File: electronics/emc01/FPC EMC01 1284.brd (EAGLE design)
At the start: 160 x 100 mm, 93 parts, among them J4 PCIE, Q1 RFP30N06LE, Q2 RFP30N06LE, Q3 RFP30N06LE, SW1 SPST_TACT-EVQQ2, U1 LM2841, U10 MCP4728, U2 A4982, U3 A4982, U4 A4982, U5 ATMEGA1284P-AU, U7 AP7313, X1 Camera FFC

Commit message: Added modular tool connectors, RasPi connector, Front Panel connector. 
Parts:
- removed D2: (no value), printrbot:SMA
- removed F1: (no value), printrbot:MINISMDC
- removed JP17: FAN, SparkFun:1X02
- removed JP2: LCD HEADER, pinhead-2:2X08SMD
- removed JP5: RPI GPIO, pinhead-2:2X13SMD
- removed JP6: HOTEND, SRG:JST_B4B-PH_HEADER
- removed MS-X, MS-Y, MS-Z: (no value), printrbot:SJ_3_CONNECTED
- removed Q1, Q2: RFP30N06LE, SparkFun:TO220V
- removed Q3: RFP30N06LE, ipc-7351-transistor:SOT95P280X135-3N
- removed R11, R36: 100, adafruit:R0805
- removed R14, R35, R6: 100k, adafruit:R0805
- removed X1: Camera FFC, con-hirose:FH12-15S-0.5SH
- added J1, J3, J5, J6, J7: (no value), !con-lstb:MA08-2
- added J11: (no value), !con-lstb:MA06-1
- added J12: (no value), !con-lstb:MA02-1
- added J8: CON-HDMI, !NJ SMT:CON-HDMI-FCI-10029449-001RLF
- added J9: CON-FFC-SFW15R, !NJ SMT:CON-FFC-SFW15R
- J2: device printrbot:PHOENIX-5MM-2POS -> !con-lstb:MA13-2
- moved J2 263.9 mm to (-125.7, -219.7)
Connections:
- net XYZENABLE renamed /XYZENABLE
- removed net !HOTBED: R11.1, R35.1
- removed net !HOTEND: R36.1, R6.1
- removed net !PWM-FAN: Q3.1, R14.1
- removed net B-THERM: U5.36
- removed net E-THERM: U5.37
- removed net HOTBED-GND: J2.P$2, Q2.2
- removed net HOTEND-GND: JP6.P1, JP6.P2, Q1.2
- removed net N$2: D2.C, F1.P$2, Q3.3
- removed net N$27: MS-X.1, U2.5
- removed net N$28: MS-X.3, U2.6
- removed net N$42: MS-Y.1, U3.5
- removed net N$43: MS-Y.3, U3.6
- removed net N$5: F1.P$1, JP17.2
- removed net N$57: MS-Z.1, U4.5
- removed net N$58: MS-Z.3, U4.6
- removed net N$7: Q2.1, R11.2
- removed net N$71: Q1.1, R36.2
- removed net PD0-RX1: U5.9
- removed net PD1-TX1: U5.10
- removed net SCK: U5.3
- removed net TOOL-DIR: U5.40
- removed net TOOL-STEP: U5.41
- removed net TOOL1-DOUT: U5.33
- removed net TOOL1-ENABLE: U5.14
- removed net TOOL2-DOUT: U5.32
- removed net TOOL2-ENABLE: U5.13
- removed net TOOL3-DOUT: U5.31
- removed net TOOL3-ENABLE: U5.12
- removed net TOOL4-AIN: U5.34
- removed net TOOL4-DOUT: U5.30
- removed net TOOL4-ENABLE: U5.11
- removed net VREF_E: U10.6
- removed net Z-ENABLE: U5.35
- new net +3V3_RASPI: J2.1, J2.17, J7.2
- new net AVR_RXD: J11.3, U5.9
- new net AVR_TXD: J11.2, U5.10
- new net DTR: J11.1
- new net LCD_/E: J2.18, J7.7
- new net LCD_DB4: J2.16, J7.9
- new net LCD_DB5: J2.11, J7.10
- new net LCD_DB6: J2.13, J7.11
- new net LCD_DB7: J2.15, J7.12
- new net LCD_RS: J2.22, J7.8
- new net PANEL_ENC_A: J2.26, J7.5
- new net PANEL_ENC_B: J2.21, J7.6
- new net PANEL_ENC_SW: J2.24, J7.4
- new net PANEL_LED_GRN: J2.19, J7.13
- new net PANEL_LED_RED: J2.12, J7.14
- new net PANEL_PUSHBTN: J2.23, J7.15
- new net RASPI_RXD: J12.1, J2.10
- new net RASPI_TXD: J12.2, J2.8
- new net TOOL1_AIN: J1.13, U5.37
- new net TOOL1_DOUT: J1.12, U5.33
- new net TOOL1_ENABLE: J1.9, U5.14
- new net TOOL2_AIN: J3.13, U5.36
- new net TOOL2_DOUT: J3.12, U5.32
- new net TOOL2_ENABLE: J3.9, U5.13
- new net TOOL3_AIN: J5.13, U5.35
- new net TOOL3_DOUT: J5.12, U5.31
- new net TOOL3_ENABLE: J5.9, U5.12
- new net TOOL4_AIN: J6.13, U5.34
- new net TOOL4_DOUT: J6.12, U5.30
- new net TOOL4_ENABLE: J6.9, U5.11
- new net TOOL_DIR: J1.11, J3.11, J5.11, J6.11, U5.40
- new net TOOL_STEP: J1.10, J3.10, J5.10, J6.10, U5.41
- new net Z_DIR: U5.42
- new net Z_STEP: U5.43
- net +5V: now also J1.14, J11.4, J2.2, J2.4, J3.14, J3.7, J5.14, J5.8, J6.14, J6.7, J6.8, J7.1, U2.5, U2.6, U3.5, U3.6, U4.5, U4.6; no longer MS-X.2, MS-Y.2, MS-Z.2
- net 12V: now also J1.1, J1.2, J3.1, J3.2, J5.1, J5.2, J6.1, J6.2; no longer J2.P$1, JP17.1, JP6.P3, JP6.P4
- net GND: now also J1.15, J1.16, J1.3, J1.4, J1.7, J1.8, J11.5, J11.6, J2.14, J2.20, J2.25, J2.6, J2.9, J3.15, J3.16, J3.3, J3.4, J3.8, J5.15, J5.16, J5.3, J5.4, J5.7, J6.15, J6.16, J6.3, J6.4, J7.16, J7.3; no longer D2.A, Q1.3, Q2.3, Q3.2, R14.2, R35.2, R6.2
- net SCL: now also J1.6, J3.6, J5.6, J6.6
- net SCLK: now also U5.3
- net SDA: now also J1.5, J3.5, J5.5, J6.5
- net Z-DIR: no longer U5.42
- net Z-STEP: no longer U5.43

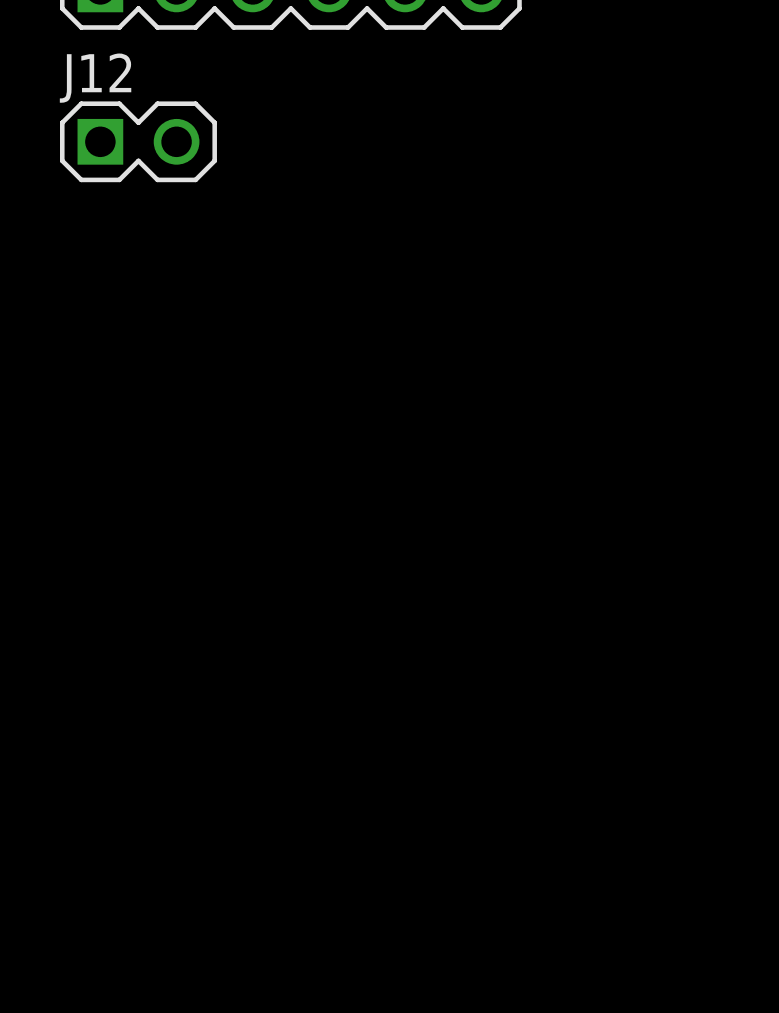
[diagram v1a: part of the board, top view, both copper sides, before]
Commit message: adding Dayton's 5958 ICSP/Power circuits to Neil's board
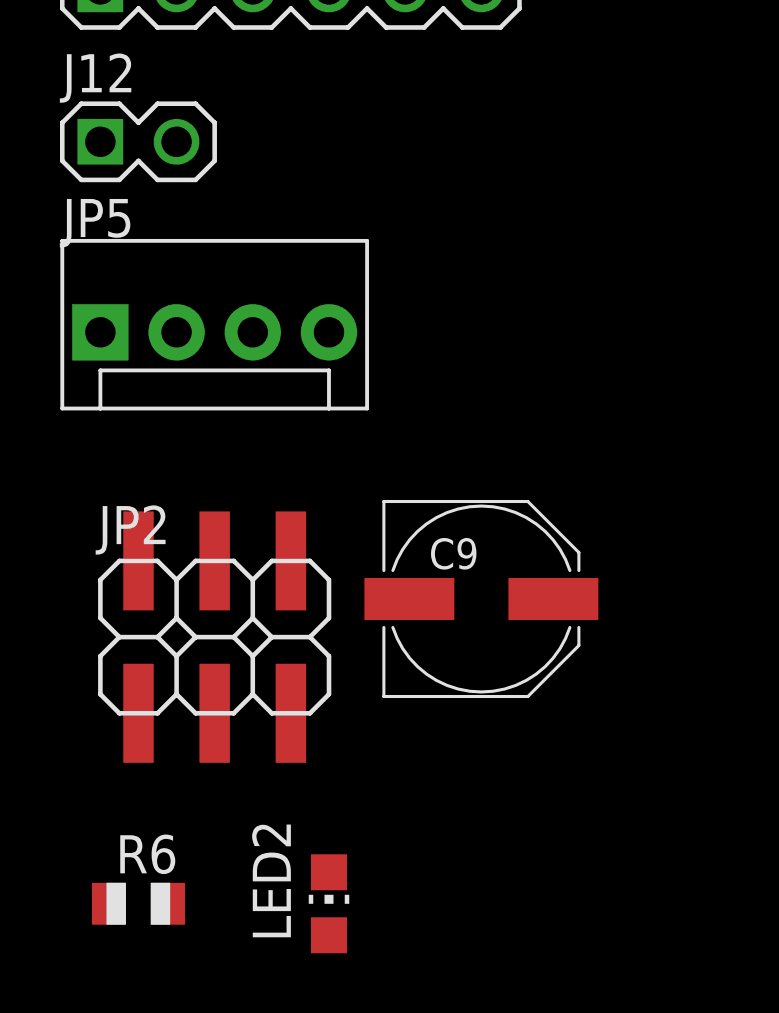
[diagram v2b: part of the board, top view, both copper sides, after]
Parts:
- added C9: 100uF, rcl:PANASONIC_D
- added JP2: ICSP, pinhead-2:2X03SMD
- added JP5: I2C, SparkFun:MOLEX-1X4
- added LED2: PWR, led:CHIP-LED0805
- added R6: 330, adafruit:R0805
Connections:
- net !RESET: now also JP2.2
- net +5V: now also JP2.5, JP5.4, R6.2
- net 12V: now also C9.+
- net GND: now also C9.-, JP2.1, JP5.3, LED2.C
- net MISO: now also JP2.6
- net MOSI: now also JP2.3
- net SCL: now also JP5.1
- net SCLK: now also JP2.4
- net SDA: now also JP5.2
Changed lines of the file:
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@@
 <?xml version="1.0" encoding="utf-8"?>
 <!DOCTYPE eagle SYSTEM "eagle.dtd">
-<eagle version="6.6.0">
+<eagle version="6.5.0">
 <drawing>
 <settings>
@@
 <element name="J11" library="!con-lstb" package="MA06-1" value="" x="-135.89" y="-257.81"/>
 <element name="J12" library="!con-lstb" package="MA02-1" value="" x="-140.97" y="-262.89"/>
+<element name="R6" library="adafruit" package="R0805" value="330" x="-140.97" y="-288.29"/>
+<element name="LED2" library="led" package="CHIP-LED0805" value="PWR" x="-134.62" y="-288.29"/>
+<element name="JP2" library="pinhead-2" package="2X03SMD" value="ICSP" x="-139.7" y="-278.13"/>
+<element name="C9" library="rcl" package="PANASONIC_D" value="100uF" x="-129.54" y="-278.13"/>
+<element name="JP5" library="SparkFun" package="MOLEX-1X4" value="I2C" x="-142.24" y="-269.24"/>
 </elements>
 <signals>
@@
 <contactref element="J11" pad="5"/>
 <contactref element="J11" pad="6"/>
+<contactref element="C9" pad="-"/>
+<contactref element="JP2" pad="1"/>
+<contactref element="LED2" pad="C"/>
+<contactref element="JP5" pad="3"/>
 <wire x1="-122.92" y1="-48.6" x2="-124.09" y2="-58.42" width="0" layer="19" extent="1-1"/>
 <wire x1="-103.82" y1="-26.67" x2="-122.92" y2="-48.6" width="0" layer="19" extent="1-1"/>
@@
 <wire x1="-132.08" y1="-257.81" x2="-138.43" y2="-228.6" width="0" layer="19" extent="1-1"/>
 <wire x1="-129.54" y1="-257.81" x2="-132.08" y2="-257.81" width="0" layer="19" extent="1-1"/>
+<wire x1="-137.16" y1="-269.24" x2="-132.08" y2="-257.81" width="0" layer="19" extent="1-1"/>
+<wire x1="-131.94" y1="-278.13" x2="-137.16" y2="-269.24" width="0" layer="19" extent="1-1"/>
+<wire x1="-134.62" y1="-287.24" x2="-131.94" y2="-278.13" width="0" layer="19" extent="1-1"/>
+<wire x1="-140.97" y1="-281.94" x2="-134.62" y2="-287.24" width="0" layer="19" extent="1-1"/>
 </signal>
 <signal name="!RESET">
 <contactref element="JP4" pad="2"/>
+<contactref element="JP2" pad="2"/>
+<wire x1="-78.74" y1="7.62" x2="-140.97" y2="-276.86" width="0" layer="19" extent="1-1"/>
 </signal>
 <signal name="12V">
@@
 <contactref element="J6" pad="1"/>
 <contactref element="J6" pad="2"/>
+<contactref element="C9" pad="+"/>
+<wire x1="-140.97" y1="-213.36" x2="-127.14" y2="-278.13" width="0" layer="19" extent="1-1"/>
 <wire x1="-140.97" y1="-210.82" x2="-140.97" y2="-213.36" width="0" layer="19" extent="1-1"/>
 <wire x1="-140.97" y1="-205.74" x2="-140.97" y2="-210.82" width="0" layer="19" extent="1-1"/>
@@
 <contactref element="JP4" pad="6"/>
 <contactref element="U5" pad="2"/>
-<wire x1="-73.66" y1="7.62" x2="72.417896875" y2="21.063946875" width="0" layer="19" extent="1-1"/>
+<contactref element="JP2" pad="6"/>
+<wire x1="-73.66" y1="7.62" x2="-135.89" y2="-276.86" width="0" layer="19" extent="1-1"/>
+<wire x1="72.417896875" y1="21.063946875" x2="-73.66" y2="7.62" width="0" layer="19" extent="1-1"/>
 </signal>
 <signal name="MOSI">
 <contactref element="JP4" pad="3"/>
 <contactref element="U5" pad="1"/>
-<wire x1="-76.2" y1="2.54" x2="71.861121875" y2="21.620721875" width="0" layer="19" extent="1-1"/>
+<contactref element="JP2" pad="3"/>
+<wire x1="-76.2" y1="2.54" x2="-138.43" y2="-281.94" width="0" layer="19" extent="1-1"/>
+<wire x1="71.861121875" y1="21.620721875" x2="-76.2" y2="2.54" width="0" layer="19" extent="1-1"/>
 </signal>
 <signal name="X-STOP">
@@
 <contactref element="JP4" pad="4"/>
 <contactref element="U5" pad="3"/>
-<wire x1="-76.2" y1="7.62" x2="72.992634375" y2="20.489209375" width="0" layer="19" extent="1-1"/>
+<contactref element="JP2" pad="4"/>
+<wire x1="-76.2" y1="7.62" x2="-138.43" y2="-276.86" width="0" layer="19" extent="1-1"/>
+<wire x1="72.992634375" y1="20.489209375" x2="-76.2" y2="7.62" width="0" layer="19" extent="1-1"/>
 </signal>
 <signal name="!XYZ-ENABLE">
@@
 <contactref element="U4" pad="5"/>
 <contactref element="J11" pad="4"/>
+<contactref element="R6" pad="2"/>
+<contactref element="JP2" pad="5"/>
+<contactref element="JP5" pad="4"/>
 <wire x1="-122.92" y1="-53" x2="-122.29" y2="-58.42" width="0" layer="19" extent="1-1"/>
 <wire x1="-121.42" y1="-53" x2="-122.92" y2="-53" width="0" layer="19" extent="1-1"/>
@@
 <wire x1="-140.97" y1="-228.6" x2="-140.97" y2="-218.44" width="0" layer="19" extent="1-1"/>
 <wire x1="-134.62" y1="-257.81" x2="-140.97" y2="-228.6" width="0" layer="19" extent="1-1"/>
+<wire x1="-134.62" y1="-269.24" x2="-134.62" y2="-257.81" width="0" layer="19" extent="1-1"/>
+<wire x1="-135.89" y1="-281.94" x2="-134.62" y2="-269.24" width="0" layer="19" extent="1-1"/>
+<wire x1="-139.97" y1="-288.29" x2="-135.89" y2="-281.94" width="0" layer="19" extent="1-1"/>
 </signal>
 <signal name="SCL" class="1">
@@
 <contactref element="J5" pad="6"/>
 <contactref element="J6" pad="6"/>
+<contactref element="JP5" pad="1"/>
 <wire x1="-34.29" y1="41.91" x2="-122.42" y2="-53" width="0" layer="19" extent="1-1"/>
 <wire x1="-135.89" y1="-187.96" x2="-122.42" y2="-53" width="0" layer="19" extent="1-1"/>
@@
 <wire x1="-135.89" y1="-203.2" x2="-135.89" y2="-195.58" width="0" layer="19" extent="1-1"/>
 <wire x1="-135.89" y1="-210.82" x2="-135.89" y2="-203.2" width="0" layer="19" extent="1-1"/>
+<wire x1="-142.24" y1="-269.24" x2="-135.89" y2="-210.82" width="0" layer="19" extent="1-1"/>
 </signal>
 <signal name="SDA" class="1">
@@
 <contactref element="J5" pad="5"/>
 <contactref element="J6" pad="5"/>
+<contactref element="JP5" pad="2"/>
 <wire x1="-31.75" y1="41.91" x2="-121.92" y2="-53" width="0" layer="19" extent="1-1"/>
 <wire x1="-135.89" y1="-190.5" x2="-121.92" y2="-53" width="0" layer="19" extent="1-1"/>
@@
 <wire x1="-135.89" y1="-205.74" x2="-135.89" y2="-198.12" width="0" layer="19" extent="1-1"/>
 <wire x1="-135.89" y1="-213.36" x2="-135.89" y2="-205.74" width="0" layer="19" extent="1-1"/>
+<wire x1="-139.7" y1="-269.24" x2="-135.89" y2="-213.36" width="0" layer="19" extent="1-1"/>
 </signal>
 <signal name="RESET">
